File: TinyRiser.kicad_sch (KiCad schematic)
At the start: 25 parts, among them J2 Bus_PCI_Express_x16, J3 Bus_M.2_Socket_M, J4 fancontrol_header, M1 Fan_4pin

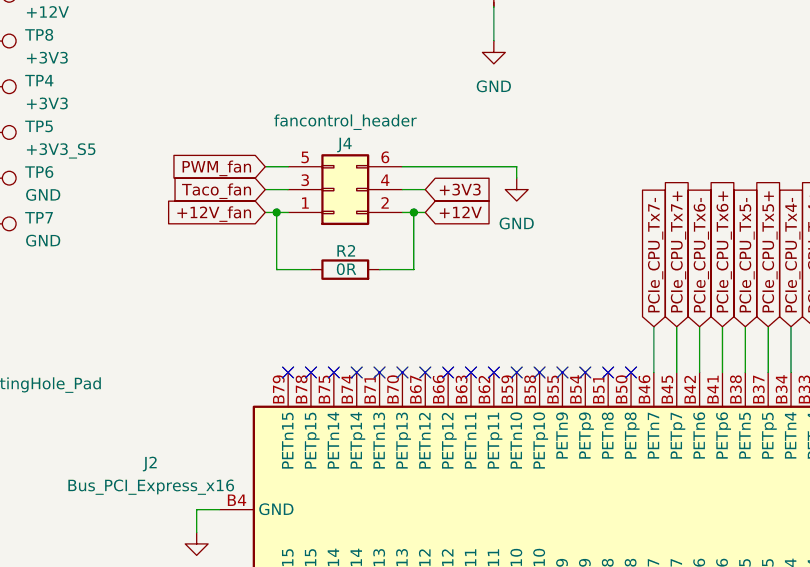
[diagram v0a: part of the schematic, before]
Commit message: Changed fan power 0R to solder jumper for easier assembly (v2.1) and added pcb ordering information
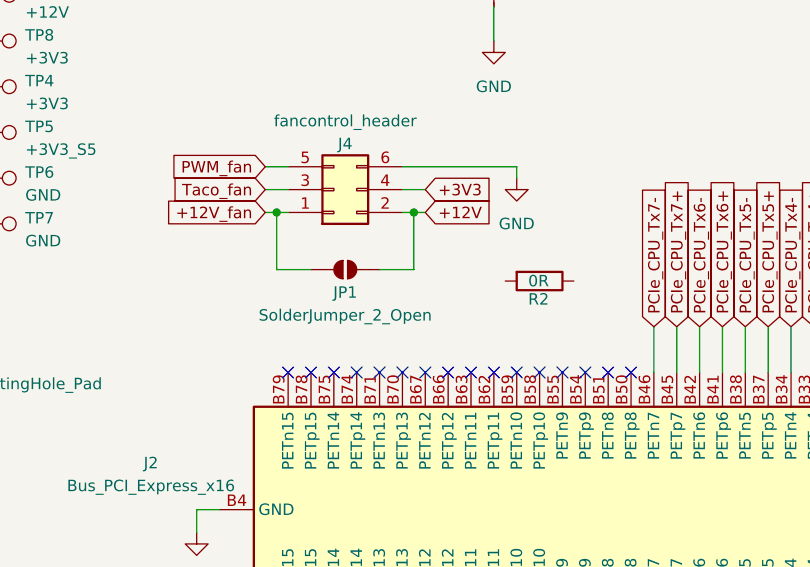
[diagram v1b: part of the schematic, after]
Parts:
- added JP1: SolderJumper_2_Open, Jumper:SolderJumper-2_P1.3mm_Open_TrianglePad1.0x1.5mm, symbol Jumper:SolderJumper_2_Open
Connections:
- net +12V: now also JP1.2 (B); no longer R2.2
- net +12V_fan: now also JP1.1 (A); no longer R2.1
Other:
- moved on the sheet: R2
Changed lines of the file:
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@@
 	(symbol
 		(lib_id "Device:R")
-		(at 210.82 63.5 90)
+		(at 232.41 64.77 270)
 		(unit 1)
 		(exclude_from_sim no)
@@
 		(dnp no)
 		(property "Reference" "R2"
-			(at 212.09 61.468 90)
+			(at 231.14 66.802 90)
 			(effects
 				(font
@@
 		)
 		(property "Value" "0R"
-			(at 212.09 63.5 90)
+			(at 231.14 64.77 90)
 			(effects
 				(font
@@
 		)
 		(property "Footprint" "Resistor_SMD:R_0805_2012Metric_Pad1.20x1.40mm_HandSolder"
-			(at 210.82 65.278 90)
+			(at 232.41 62.992 90)
 			(effects
 				(font
@@
 		)
 		(property "Datasheet" "~"
-			(at 210.82 63.5 0)
-			(effects
-				(font
-					(size 1.27 1.27)
-				)
-				(hide yes)
-			)
-		)
-		(property "Description" ""
-			(at 210.82 63.5 0)
+			(at 232.41 64.77 0)
+			(effects
+				(font
+					(size 1.27 1.27)
+				)
+				(hide yes)
+			)
+		)
+		(property "Description" ""
+			(at 232.41 64.77 0)
 			(effects
 				(font
@@
 					(unit 1)
 				)
+			)
+		)
+	)
+	(symbol
+		(lib_id "Jumper:SolderJumper_2_Open")
+		(at 210.82 63.5 0)
+		(unit 1)
+		(exclude_from_sim yes)
+		(in_bom no)
+		(on_board yes)
+		(dnp no)
+		(property "Reference" "JP1"
+			(at 210.82 66.04 0)
+			(effects
+				(font
+					(size 1.27 1.27)
+				)
+			)
+		)
+		(property "Value" "SolderJumper_2_Open"
+			(at 210.82 68.58 0)
+			(effects
+				(font
+					(size 1.27 1.27)
+				)
+			)
+		)
+		(property "Footprint" "Jumper:SolderJumper-2_P1.3mm_Open_TrianglePad1.0x1.5mm"
+			(at 210.82 63.5 0)
+			(effects
+				(font
+					(size 1.27 1.27)
+				)
+				(hide yes)
+			)
+		)
+		(property "Datasheet" "~"
+			(at 210.82 63.5 0)
+			(effects
+				(font
+					(size 1.27 1.27)
+				)
+				(hide yes)
+			)
+		)
+		(property "Description" "Solder Jumper, 2-pole, open"
+			(at 210.82 63.5 0)
+			(effects
+				(font
+					(size 1.27 1.27)
+				)
+				(hide yes)
+			)
+		)
+		(pin "2"
+		)
+		(pin "1"
+		)
+		(instances
+			(project "TinyRiser"
+				(path "/881240ea-c4b5-4af2-848a-893b6d69814c"
+					(reference "JP1")
+					(unit 1)
+				)

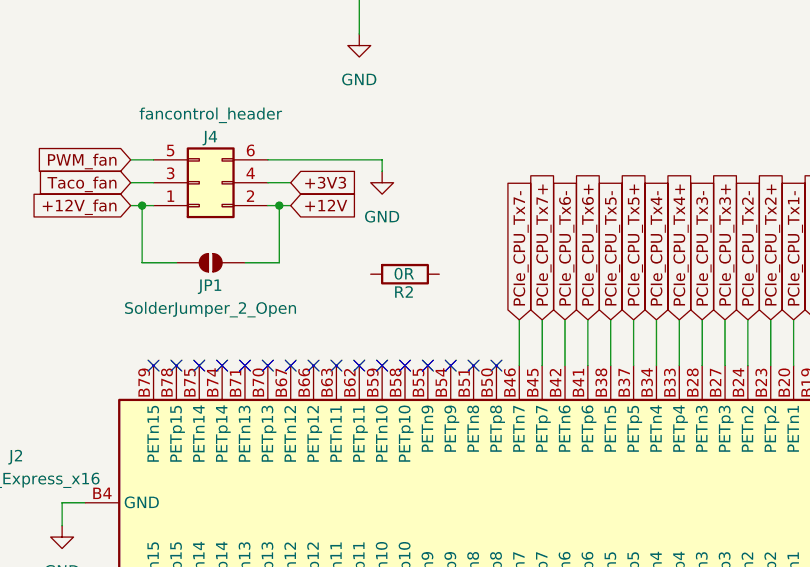
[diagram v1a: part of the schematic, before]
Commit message: Increased power rail testpoint hole size and decreased screwpost hole size for better fit
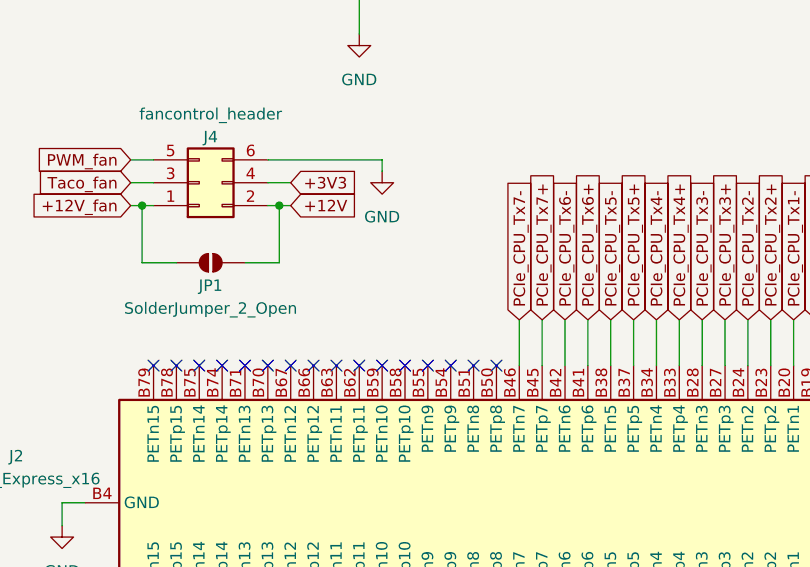
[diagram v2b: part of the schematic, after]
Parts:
- removed R2: 0R, Resistor_SMD:R_0805_2012Metric_Pad1.20x1.40mm_HandSolder, symbol Device:R
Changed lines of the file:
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@@
-	)
-	(symbol
-		(lib_id "Device:R")
-		(at 232.41 64.77 270)
-		(unit 1)
-		(exclude_from_sim no)
-		(in_bom yes)
-		(on_board yes)
-		(dnp no)
-		(property "Reference" "R2"
-			(at 231.14 66.802 90)
-			(effects
-				(font
-					(size 1.27 1.27)
-				)
-				(justify left)
-			)
-		)
-		(property "Value" "0R"
-			(at 231.14 64.77 90)
-			(effects
-				(font
-					(size 1.27 1.27)
-				)
-				(justify left)
-			)
-		)
-		(property "Footprint" "Resistor_SMD:R_0805_2012Metric_Pad1.20x1.40mm_HandSolder"
-			(at 232.41 62.992 90)
-			(effects
-				(font
-					(size 1.27 1.27)
-				)
-				(hide yes)
-			)
-		)
-		(property "Datasheet" "~"
-			(at 232.41 64.77 0)
-			(effects
-				(font
-					(size 1.27 1.27)
-				)
-				(hide yes)
-			)
-		)
-		(property "Description" ""
-			(at 232.41 64.77 0)
-			(effects
-				(font
-					(size 1.27 1.27)
-				)
-				(hide yes)
-			)
-		)
-		(pin "1"
-		)
-		(pin "2"
-		)
-		(instances
-			(project "TinyRiser"
-				(path "/881240ea-c4b5-4af2-848a-893b6d69814c"
-					(reference "R2")
-					(unit 1)
-				)
-			)
-		)
 	)
 	(symbol
